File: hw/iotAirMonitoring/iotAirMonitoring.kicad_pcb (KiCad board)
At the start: 2 copper layers, 100 x 100 mm, 130 parts, among them J1 MQ-7, J10 USB_DATA, J11 PWR, J12 USB_B_Micro, J13 PM1003, J14 Battery_shield, J15 SMA, J2 VEML7700, J3 SHT40, J4 PROGRAMMER, J5 ML8511, J6 EN_3V3_PROGRAMMER, J7 BMP388, J8 PMS5003, J9 USB_C_Receptacle_USB2.0, Q1 MMBT3904, Q10 AO3401A, Q11 2N7002, Q12 AO3401A, Q13 2N7002, Q14 AO3401A, Q15 2N7002, Q16 2N7002, Q17 2N7002, Q2 MMBT3904, Q3 AO3401A, Q4 2N7002, Q5 AO3401A, Q6 2N7002, Q7 AO3401A, Q8 2N7002, Q9 AO3401A, SW1 PWR_ON, SW2 PWR_OFF, SW3 RESET, SW4 SW_Push, U1 ESP32-WROOM-32, U2 MCP3202-BI/SN, U3 AMS1117-3.3, U4 TPS54331, U5 RFM95W-868S2

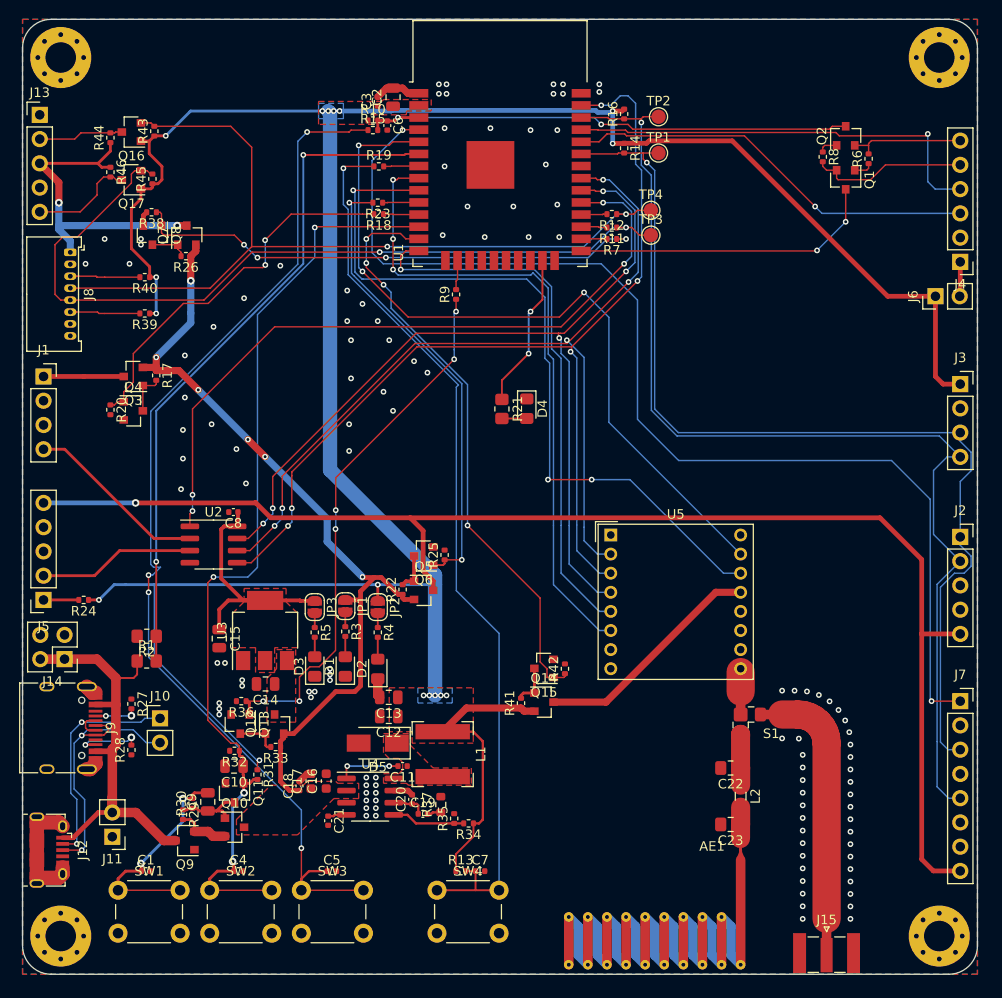
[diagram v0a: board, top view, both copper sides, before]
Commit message: Add TestPads, improve silkscreen
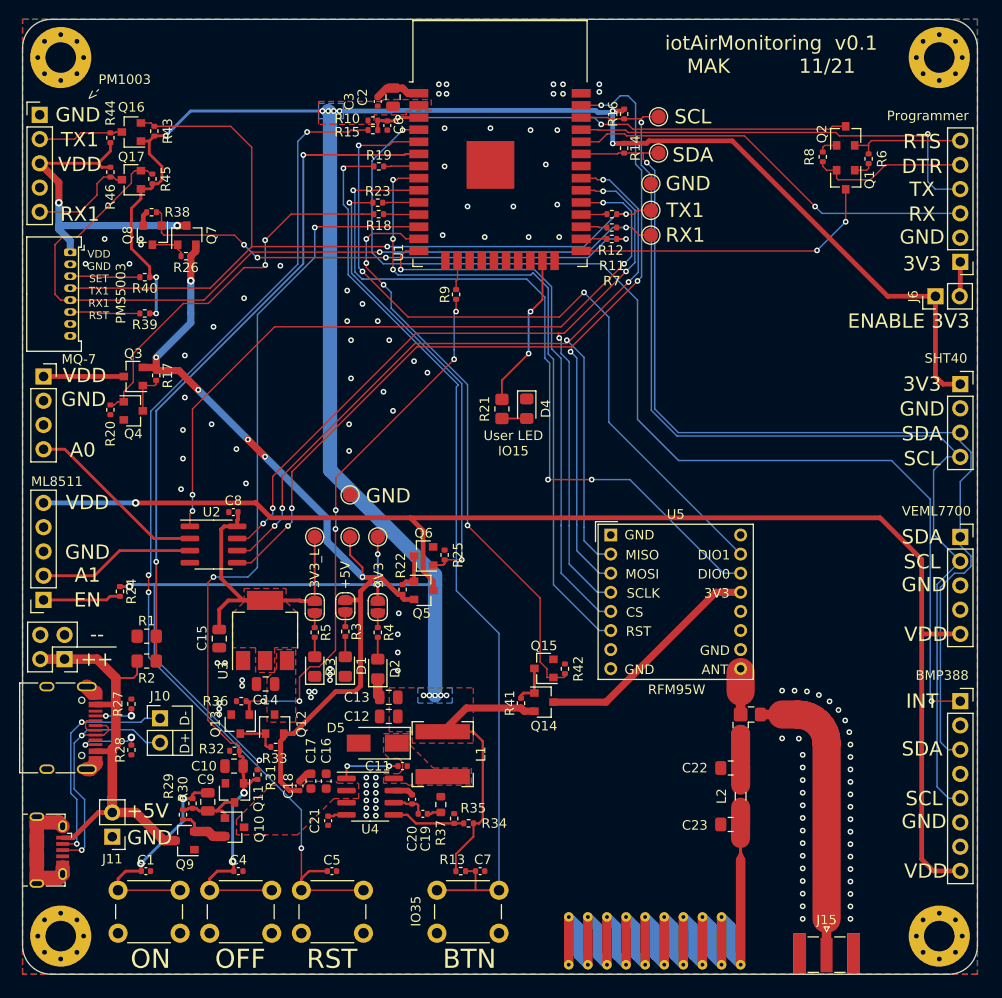
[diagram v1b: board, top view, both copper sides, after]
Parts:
- added TP5: TP_VDD, TestPoint:TestPoint_Pad_D1.5mm, F.Cu at (190.3, 99.2)
- added TP6: TP_3V3, TestPoint:TestPoint_Pad_D1.5mm, F.Cu at (193.2, 99.2)
- added TP7: TP_3V3_L, TestPoint:TestPoint_Pad_D1.5mm, F.Cu at (186.6, 99.2)
- added TP8: TP_GND, TestPoint:TestPoint_Pad_D1.5mm, F.Cu at (221.8, 62.2)
- added TP9: TP_GND, TestPoint:TestPoint_Pad_D1.5mm, F.Cu at (190.3, 94.8)
- moved R24 3.90 mm to (166.2, 104.9), turned to 270 degrees
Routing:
- net 3V3_L: track 26.5 -> 33.2 mm
- net VDD: track 86.1 -> 90.8 mm
- net /interface/UV_EN: track 3.69 -> 8.16 mm
- net Net-(C5-Pad1): track 111.6 -> 110.1 mm
- net 3V3: track 288.0 -> 289.1 mm, vias 17 -> 18
- net GND: vias 116 -> 120
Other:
- board text added: "++"
- board text added: "+5V"
- board text added: "--"
- board text added: "3V3"
- board text added: "3V3_L"
- board text added: "<-"
- board text added: "A0"
- board text added: "A1"
- board text added: "ANT"
- board text added: "BMP388"
- board text added: "BTN"
- board text added: "CS"
- board text added: "D+"
- board text added: "D-"
- board text added: "DIO0"
- board text added: "DIO1"
- board text added: "DTR"
- board text added: "EN"
- board text added: "ENABLE 3V3"
- board text added: "GND"
- board text added: "INT"
- board text added: "IO35"
- board text added: "MISO"
- board text added: "ML8511"
- board text added: "MOSI"
- board text added: "MQ-7"
- board text added: "OFF"
- board text added: "ON"
- board text added: "PM1003"
- board text added: "PMS5003"
- board text added: "Programmer"
- board text added: "RFM95W"
- board text added: "RST"
- board text added: "RTS"
- board text added: "RX"
- board text added: "RX1"
- board text added: "SCL"
- board text added: "SCLK"
- board text added: "SDA"
- board text added: "SHT40"
- board text added: "TX"
- board text added: "TX1"
- board text added: "User LED IO15"
- board text added: "VDD"
- board text added: "VDD GND SET TX1 RX1 RST"
- board text added: "VEML7700"
- board text added: "iotAirMonitoring v0.1 MAK 11/21"

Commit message: Add JLCPCB assembly correction, generate gerber data
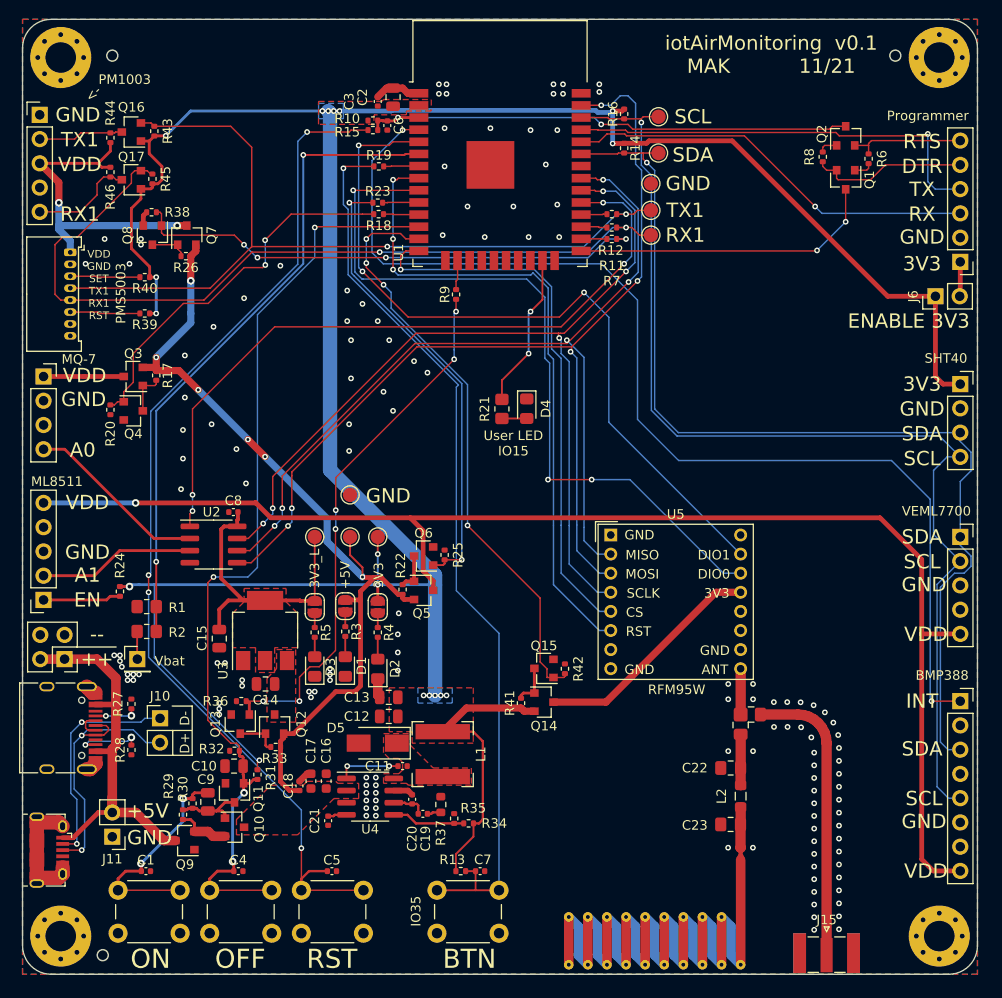
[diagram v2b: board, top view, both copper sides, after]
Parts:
- added J16: Battery_voltage, Connector_PinHeader_2.54mm:PinHeader_1x01_P2.54mm_Vertical, F.Cu at (168.0, 112.0)
- moved R1 3.10 mm to (169.0, 109.1)
- moved R2 3.10 mm to (169.0, 106.5)
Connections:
- R1 pad 1: USB_VDD -> Net-(J16-Pad1)
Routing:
- net USB_VDD: track 46.5 -> 42.7 mm
- net ADC_VIN: track 71.5 -> 68.4 mm
- net Net-(J16-Pad1): track 0.00 -> 2.91 mm
- net Net-(AE1-Pad1): track 4.66 -> 7.19 mm
- net Net-(S1-Pad1): track 6.85 -> 4.80 mm
- net GND: vias 120 -> 139
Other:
- outline, holes or cut-outs redrawn
- board text added: "JLCJLCJLCJLC"
- board text added: "Vbat"
